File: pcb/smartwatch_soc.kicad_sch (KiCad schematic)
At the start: 37 parts, among them J1 Battery Socket, J2 USB_A, Q1 PN2222A, Q2 PN2222A, Q3 PN2222A, SW1 EN_Switch, SW2 Button, SW3 Button, SW4 Button, SW5 Button, U1 ESP32-S3-MINI-1U, U2 LSM6DS3, U3 OLED_Display, U5 CP2102N-Axx-xQFN20

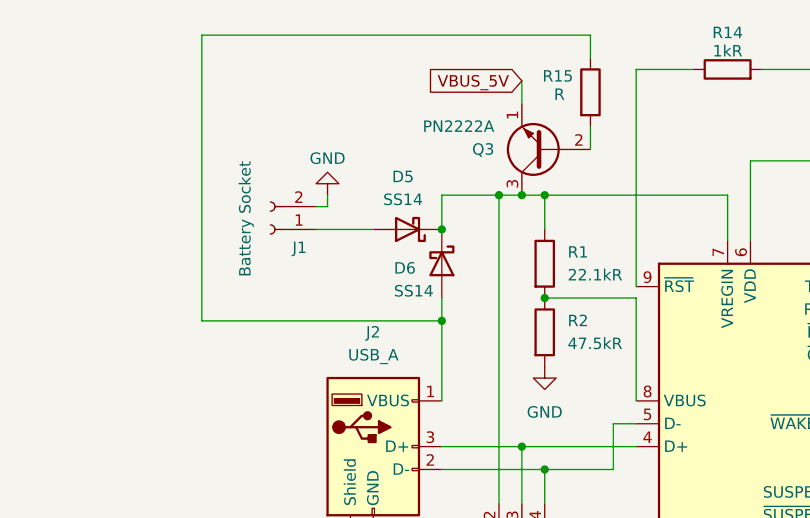
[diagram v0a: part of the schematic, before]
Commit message: use tht instead of smd for resistors, capacitors
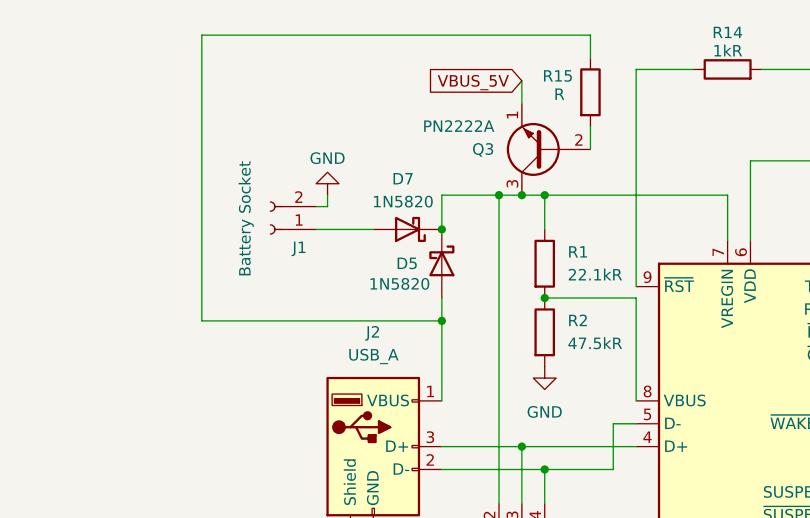
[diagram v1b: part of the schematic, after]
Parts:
- removed D5, D6: SS14, Diode_SMD:D_SMA, symbol Diode:SS14
- added D5, D7: 1N5820, Diode_THT:D_DO-201AD_P15.24mm_Horizontal, symbol Diode:1N5820
- D2, D3, D4: footprint LED_SMD:LED_0201_0603Metric -> LED_THT:LED_D2.0mm_W4.0mm_H2.8mm_FlatTop
- R1, R10, R11, R12, R13, R14, R15, R2, R3, R4, R5, R6, R7, R8, R9: footprint Resistor_SMD:R_0201_0603Metric -> Resistor_THT:R_Axial_DIN0204_L3.6mm_D1.6mm_P2.54mm_Vertical
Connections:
- net at D1.2 (K), Q3.3 (C), R1.1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: now also D5.1 (K), D7.1 (K)
- net at J1.1 (Pin_1): now also D7.2 (A)
- net at J2.1 (VBUS), R15.1: now also D5.2 (A)
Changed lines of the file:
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@@
 	)
 	(junction
+		(at 161.29 35.56)
+		(diameter 0)
+		(color 0 0 0 0)
+	)
+	(junction
 		(at 238.76 144.78)
 		(diameter 0)
@@
 	)
 	(junction
-		(at 161.29 35.56)
-		(diameter 0)
-		(color 0 0 0 0)
-	)
-	(junction
 		(at 73.66 167.64)
 		(diameter 0)
@@
 			)
 		)
-		(property "Footprint" "LED_SMD:LED_0201_0603Metric"
+		(property "Footprint" "LED_THT:LED_D2.0mm_W4.0mm_H2.8mm_FlatTop"
 			(at 256.54 144.78 0)
 			(effects
@@
 			)
 		)
-		(property "Footprint" "Resistor_SMD:R_0201_0603Metric"
+		(property "Footprint" "Resistor_THT:R_Axial_DIN0204_L3.6mm_D1.6mm_P2.54mm_Vertical"
 			(at 71.882 173.99 90)
 			(effects
@@
 	)
 	(symbol
-		(lib_id "Diode:SS14")
-		(at 157.48 35.56 180)
-		(unit 1)
-		(exclude_from_sim no)
-		(in_bom yes)
-		(on_board yes)
-		(dnp no)
-		(property "Reference" "D5"
-			(at 156.972 29.718 0)
-			(effects
-				(font
-					(size 1.27 1.27)
-				)
-			)
-		)
-		(property "Value" "SS14"
-			(at 156.972 32.258 0)
-			(effects
-				(font
-					(size 1.27 1.27)
-				)
-			)
-		)
-		(property "Footprint" "Diode_SMD:D_SMA"
-			(at 157.48 31.115 0)
-			(effects
-				(font
-					(size 1.27 1.27)
-				)
-				(hide yes)
-			)
-		)
-		(property "Datasheet" "https://www.vishay.com/docs/88746/ss12.pdf"
-			(at 157.48 35.56 0)
-			(effects
-				(font
-					(size 1.27 1.27)
-				)
-				(hide yes)
-			)
-		)
-		(property "Description" "40V 1A Schottky Diode, SMA"
-			(at 157.48 35.56 0)
-			(effects
-				(font
-					(size 1.27 1.27)
-				)
-				(hide yes)
-			)
-		)
-		(pin "2"
-		)
-		(pin "1"
-		)
-		(instances
-			(project ""
-				(path "/35fbcf8c-23e2-4364-8111-b69121d03e91"
-					(reference "D5")
-					(unit 1)
-				)
-			)
-		)
-	)
-	(symbol
 		(lib_id "Connector:USB_A")
 		(at 153.67 59.69 0)
@@
 			)
 		)
-		(property "Footprint" "Resistor_SMD:R_0201_0603Metric"
+		(property "Footprint" "Resistor_THT:R_Axial_DIN0204_L3.6mm_D1.6mm_P2.54mm_Vertical"
 			(at 170.942 46.99 90)
 			(effects
@@
 			)
 		)
-		(property "Footprint" "Resistor_SMD:R_0201_0603Metric"
+		(property "Footprint" "Resistor_THT:R_Axial_DIN0204_L3.6mm_D1.6mm_P2.54mm_Vertical"
 			(at 50.292 173.99 90)
 			(effects
@@
 			)
 		)
-		(property "Footprint" "Resistor_SMD:R_0201_0603Metric"
+		(property "Footprint" "Resistor_THT:R_Axial_DIN0204_L3.6mm_D1.6mm_P2.54mm_Vertical"
 			(at 214.63 66.548 90)
 			(effects
@@
 			)
 		)
-		(property "Footprint" "Resistor_SMD:R_0201_0603Metric"
+		(property "Footprint" "Resistor_THT:R_Axial_DIN0204_L3.6mm_D1.6mm_P2.54mm_Vertical"
 			(at 227.33 113.538 90)
 			(effects
@@
 			)
 		)
-		(property "Footprint" "Resistor_SMD:R_0201_0603Metric"
+		(property "Footprint" "Resistor_THT:R_Axial_DIN0204_L3.6mm_D1.6mm_P2.54mm_Vertical"
 			(at 29.972 173.99 90)
 			(effects
@@
 			)
 		)
-		(property "Footprint" "Resistor_SMD:R_0201_0603Metric"
+		(property "Footprint" "Resistor_THT:R_Axial_DIN0204_L3.6mm_D1.6mm_P2.54mm_Vertical"
 			(at 176.022 20.32 90)
 			(effects
@@
 			)
 		)
-		(property "Footprint" "Resistor_SMD:R_0201_0603Metric"
+		(property "Footprint" "Resistor_THT:R_Axial_DIN0204_L3.6mm_D1.6mm_P2.54mm_Vertical"
 			(at 248.92 107.188 90)
 			(effects
@@
 			)
 		)
-		(property "Footprint" "Resistor_SMD:R_0201_0603Metric"
+		(property "Footprint" "Resistor_THT:R_Axial_DIN0204_L3.6mm_D1.6mm_P2.54mm_Vertical"
 			(at 236.982 139.7 90)
 			(effects
@@
 			)
 		)
-		(property "Footprint" "Resistor_SMD:R_0201_0603Metric"
+		(property "Footprint" "Resistor_THT:R_Axial_DIN0204_L3.6mm_D1.6mm_P2.54mm_Vertical"
 			(at 170.942 39.37 90)
 			(effects
@@
 	)
 	(symbol
+		(lib_id "Diode:1N5820")
+		(at 161.29 39.37 270)
+		(unit 1)
+		(exclude_from_sim no)
+		(in_bom yes)
+		(on_board yes)
+		(dnp no)
+		(property "Reference" "D5"
+			(at 156.21 39.37 90)
+			(effects
+				(font
+					(size 1.27 1.27)
+				)
+				(justify left)
+			)
+		)
+		(property "Value" "1N5820"
+			(at 153.162 41.656 90)
+			(effects
+				(font
+					(size 1.27 1.27)
+				)
+				(justify left)
+			)
+		)
+		(property "Footprint" "Diode_THT:D_DO-201AD_P15.24mm_Horizontal"
+			(at 156.845 39.37 0)
+			(effects
+				(font
+					(size 1.27 1.27)
+				)
+				(hide yes)
+			)
+		)
+		(property "Datasheet" "http://www.vishay.com/docs/88526/1n5820.pdf"
+			(at 161.29 39.37 0)
+			(effects
+				(font
+					(size 1.27 1.27)
+				)
+				(hide yes)
+			)
+		)
+		(property "Description" "20V 3A Schottky Barrier Rectifier Diode, DO-201AD"
+			(at 161.29 39.37 0)
+			(effects
+				(font
+					(size 1.27 1.27)
+				)
+				(hide yes)
+			)
+		)
+		(pin "2"
+		)
+		(pin "1"
+		)
+		(instances
+			(project "smartwatch_soc"
+				(path "/35fbcf8c-23e2-4364-8111-b69121d03e91"
+					(reference "D5")
+					(unit 1)
+				)
+			)
+		)
+	)
+	(symbol
 		(lib_id "Connector:Conn_01x02_Socket")
 		(at 142.24 35.56 180)
@@
 			)
 		)
-		(property "Footprint" "Resistor_SMD:R_0201_0603Metric"
+		(property "Footprint" "Resistor_THT:R_Axial_DIN0204_L3.6mm_D1.6mm_P2.54mm_Vertical"
 			(at 248.92 146.558 90)
 			(effects
@@
 			)
 		)
-		(property "Footprint" "Resistor_SMD:R_0201_0603Metric"
+		(property "Footprint" "Resistor_THT:R_Axial_DIN0204_L3.6mm_D1.6mm_P2.54mm_Vertical"
 			(at 227.33 152.908 90)
 			(effects
@@
 			)
 		)
-		(property "Footprint" "Resistor_SMD:R_0201_0603Metric"
+		(property "Footprint" "Resistor_THT:R_Axial_DIN0204_L3.6mm_D1.6mm_P2.54mm_Vertical"
 			(at 92.202 173.99 90)
 			(effects
@@
 			)
 		)
-		(property "Footprint" "LED_SMD:LED_0201_0603Metric"
+		(property "Footprint" "LED_THT:LED_D2.0mm_W4.0mm_H2.8mm_FlatTop"
 			(at 256.54 105.41 0)
 			(effects
@@
 	)
 	(symbol
-		(lib_id "Diode:SS14")
-		(at 161.29 39.37 270)
-		(unit 1)
-		(exclude_from_sim no)
-		(in_bom yes)
-		(on_board yes)
-		(dnp no)
-		(property "Reference" "D6"
-			(at 155.956 39.878 90)
-			(effects
-				(font
-					(size 1.27 1.27)
-				)
-				(justify left)
-			)
-		)
-		(property "Value" "SS14"
-			(at 155.956 42.418 90)
-			(effects
-				(font
-					(size 1.27 1.27)
-				)
-				(justify left)
-			)
-		)
-		(property "Footprint" "Diode_SMD:D_SMA"
-			(at 156.845 39.37 0)
-			(effects
-				(font
-					(size 1.27 1.27)
-				)
-				(hide yes)
-			)
-		)
-		(property "Datasheet" "https://www.vishay.com/docs/88746/ss12.pdf"
-			(at 161.29 39.37 0)
-			(effects
-				(font
-					(size 1.27 1.27)
-				)
-				(hide yes)
-			)
-		)
-		(property "Description" "40V 1A Schottky Diode, SMA"
-			(at 161.29 39.37 0)
-			(effects
-				(font
-					(size 1.27 1.27)
-				)
-				(hide yes)
-			)
-		)
-		(pin "2"
-		)
-		(pin "1"
-		)
-		(instances
-			(project "smartwatch_soc"
-				(path "/35fbcf8c-23e2-4364-8111-b69121d03e91"
-					(reference "D6")
-					(unit 1)
-				)
-			)
-		)
-	)
-	(symbol
 		(lib_id "Switch:CK_KMS2xxG")
 		(at 73.66 160.02 90)
@@
 			)
 		)
-		(property "Footprint" "Resistor_SMD:R_0201_0603Metric"
+		(property "Footprint" "Resistor_THT:R_Axial_DIN0204_L3.6mm_D1.6mm_P2.54mm_Vertical"
 			(at 193.04 19.558 90)
 			(effects
@@
 			)
 		)
-		(property "Footprint" "LED_SMD:LED_0201_0603Metric"
+		(property "Footprint" "LED_THT:LED_D2.0mm_W4.0mm_H2.8mm_FlatTop"
 			(at 222.25 64.77 0)
 			(effects
@@
 			)
 		)
-		(property "Footprint" "Resistor_SMD:R_0201_0603Metric"
+		(property "Footprint" "Resistor_THT:R_Axial_DIN0204_L3.6mm_D1.6mm_P2.54mm_Vertical"
 			(at 236.982 100.33 90)
 			(effects
@@
 					(unit 1)
 				)
+			)
+		)
+	)
+	(symbol
+		(lib_id "Diode:1N5820")
+		(at 157.48 35.56 180)
+		(unit 1)
+		(exclude_from_sim no)
+		(in_bom yes)
+		(on_board yes)
+		(dnp no)
+		(property "Reference" "D7"
+			(at 156.972 29.972 0)
+			(effects
+				(font
+					(size 1.27 1.27)
+				)
+			)
+		)
+		(property "Value" "1N5820"
+			(at 156.972 32.512 0)
+			(effects
+				(font
+					(size 1.27 1.27)
+				)
+			)
+		)
+		(property "Footprint" "Diode_THT:D_DO-201AD_P15.24mm_Horizontal"
+			(at 157.48 31.115 0)
+			(effects
+				(font
+					(size 1.27 1.27)
+				)
+				(hide yes)
+			)
+		)
+		(property "Datasheet" "http://www.vishay.com/docs/88526/1n5820.pdf"
+			(at 157.48 35.56 0)
+			(effects
+				(font
+					(size 1.27 1.27)
+				)
+				(hide yes)
+			)
+		)
+		(property "Description" "20V 3A Schottky Barrier Rectifier Diode, DO-201AD"
+			(at 157.48 35.56 0)
+			(effects
+				(font
+					(size 1.27 1.27)
+				)
+				(hide yes)
+			)
+		)
+		(pin "2"
+		)
+		(pin "1"
+		)
+		(instances
+			(project ""
+				(path "/35fbcf8c-23e2-4364-8111-b69121d03e91"
+					(reference "D7")
+					(unit 1)
+				)

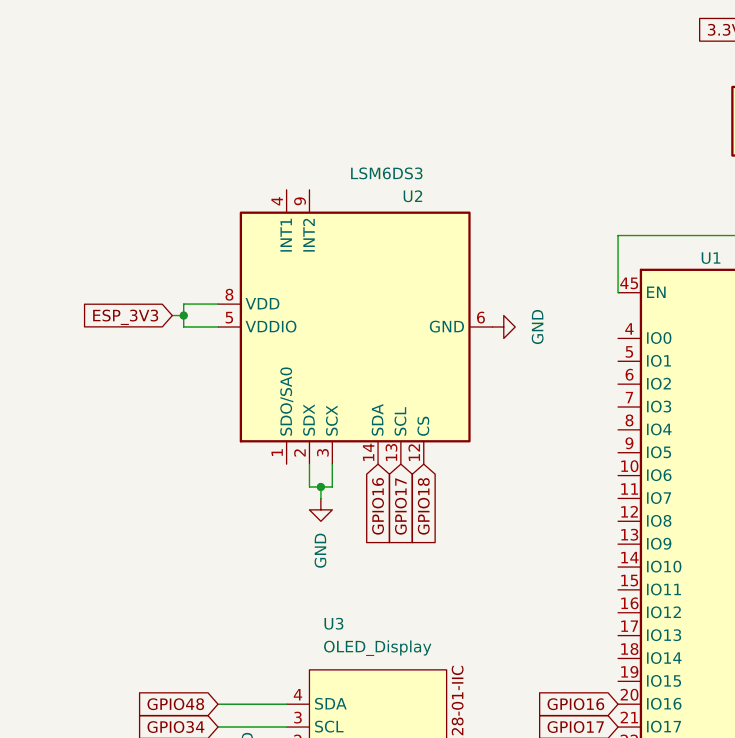
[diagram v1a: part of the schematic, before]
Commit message: added decoupling capacitors for accelerometer
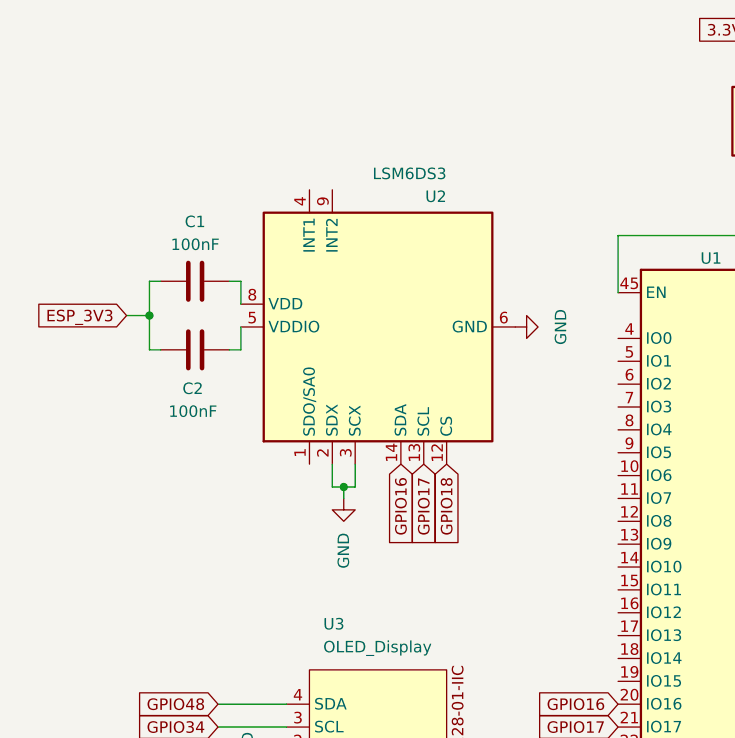
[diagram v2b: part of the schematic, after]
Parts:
- added C1, C2: 100nF, symbol Device:C
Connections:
- net ESP_3V3: now also C1.1, C2.1; no longer U2.5 (VDDIO), U2.8 (VDD)
- new net: C2.2, U2.5 (VDDIO)
- new net: C1.2, U2.8 (VDD)
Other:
- moved on the sheet: U2
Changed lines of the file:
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@@
 	)
 	(junction
-		(at 46.99 104.14)
+		(at 49.53 104.14)
 		(diameter 0)
 		(color 0 0 0 0)
 	)
 	(junction
-		(at 31.75 85.09)
+		(at 27.94 85.09)
 		(diameter 0)
 		(color 0 0 0 0)
@@
 	(wire
 		(pts
-			(xy 46.99 105.41) (xy 46.99 104.14)
+			(xy 49.53 105.41) (xy 49.53 104.14)
 		)
 		(stroke
@@
 	(wire
 		(pts
-			(xy 48.26 101.6) (xy 48.26 104.14)
+			(xy 50.8 101.6) (xy 50.8 104.14)
 		)
 		(stroke
@@
 	(wire
 		(pts
-			(xy 45.72 104.14) (xy 46.99 104.14)
+			(xy 48.26 104.14) (xy 49.53 104.14)
 		)
 		(stroke
@@
 	(wire
 		(pts
-			(xy 35.56 86.36) (xy 31.75 86.36)
+			(xy 38.1 88.9) (xy 36.83 88.9)
 		)
 		(stroke
@@
 	(wire
 		(pts
+			(xy 38.1 88.9) (xy 38.1 86.36)
+		)
+		(stroke
+			(width 0)
+			(type default)
+		)
+	)
+	(wire
+		(pts
 			(xy 116.84 86.36) (xy 118.11 86.36)
 		)
@@
 	(wire
 		(pts
-			(xy 31.75 85.09) (xy 31.75 86.36)
+			(xy 27.94 85.09) (xy 27.94 88.9)
 		)
 		(stroke
@@
 	(wire
 		(pts
-			(xy 31.75 83.82) (xy 35.56 83.82)
+			(xy 27.94 81.28) (xy 29.21 81.28)
 		)
 		(stroke
@@
 	(wire
 		(pts
-			(xy 31.75 83.82) (xy 31.75 85.09)
+			(xy 27.94 81.28) (xy 27.94 85.09)
+		)
+		(stroke
+			(width 0)
+			(type default)
+		)
+	)
+	(wire
+		(pts
+			(xy 36.83 81.28) (xy 38.1 81.28)
 		)
 		(stroke
@@
 	(wire
 		(pts
-			(xy 31.75 85.09) (xy 30.48 85.09)
+			(xy 27.94 85.09) (xy 25.4 85.09)
 		)
 		(stroke
@@
 	(wire
 		(pts
-			(xy 48.26 104.14) (xy 46.99 104.14)
+			(xy 50.8 104.14) (xy 49.53 104.14)
 		)
 		(stroke
@@
 	(wire
 		(pts
-			(xy 45.72 101.6) (xy 45.72 104.14)
+			(xy 48.26 101.6) (xy 48.26 104.14)
 		)
 		(stroke
@@
 	(wire
 		(pts
+			(xy 38.1 81.28) (xy 38.1 83.82)
+		)
+		(stroke
+			(width 0)
+			(type default)
+		)
+	)
+	(wire
+		(pts
 			(xy 153.67 69.85) (xy 153.67 76.2)
 		)
@@
 	(wire
 		(pts
+			(xy 29.21 88.9) (xy 27.94 88.9)
+		)
+		(stroke
+			(width 0)
+			(type default)
+		)
+	)
+	(wire
+		(pts
 			(xy 52.07 151.13) (xy 52.07 154.94)
 		)
@@
 	(global_label "GPIO18"
 		(shape input)
-		(at 58.42 101.6 270)
+		(at 60.96 101.6 270)
 		(fields_autoplaced yes)
 		(effects
@@
 		)
 		(property "Intersheetrefs" "${INTERSHEET_REFS}"
-			(at 58.42 111.4795 90)
+			(at 60.96 111.4795 90)
 			(effects
 				(font
@@
 	(global_label "GPIO17"
 		(shape input)
-		(at 55.88 101.6 270)
+		(at 58.42 101.6 270)
 		(fields_autoplaced yes)
 		(effects
@@
 		)
 		(property "Intersheetrefs" "${INTERSHEET_REFS}"
-			(at 55.88 111.4795 90)
+			(at 58.42 111.4795 90)
 			(effects
 				(font
@@
 	(global_label "GPIO16"
 		(shape input)
-		(at 53.34 101.6 270)
+		(at 55.88 101.6 270)
 		(fields_autoplaced yes)
 		(effects
@@
 		)
 		(property "Intersheetrefs" "${INTERSHEET_REFS}"
-			(at 53.34 111.4795 90)
+			(at 55.88 111.4795 90)
 			(effects
 				(font
@@
 	(global_label "ESP_3V3"
 		(shape input)
-		(at 30.48 85.09 180)
+		(at 25.4 85.09 180)
 		(fields_autoplaced yes)
 		(effects
@@
 		)
 		(property "Intersheetrefs" "${INTERSHEET_REFS}"
-			(at 19.3911 85.09 0)
+			(at 14.3111 85.09 0)
 			(effects
 				(font
@@
 	)
 	(symbol
+		(lib_id "Device:C")
+		(at 33.02 88.9 90)
+		(unit 1)
+		(exclude_from_sim no)
+		(in_bom yes)
+		(on_board yes)
+		(dnp no)
+		(property "Reference" "C2"
+			(at 32.766 93.218 90)
+			(effects
+				(font
+					(size 1.27 1.27)
+				)
+			)
+		)
+		(property "Value" "100nF"
+			(at 32.766 95.758 90)
+			(effects
+				(font
+					(size 1.27 1.27)
+				)
+			)
+		)
+		(property "Footprint" ""
+			(at 36.83 87.9348 0)
+			(effects
+				(font
+					(size 1.27 1.27)
+				)
+				(hide yes)
+			)
+		)
+		(property "Datasheet" "~"
+			(at 33.02 88.9 0)
+			(effects
+				(font
+					(size 1.27 1.27)
+				)
+				(hide yes)
+			)
+		)
+		(property "Description" "Unpolarized capacitor"
+			(at 33.02 88.9 0)
+			(effects
+				(font
+					(size 1.27 1.27)
+				)
+				(hide yes)
+			)
+		)
+		(pin "2"
+		)
+		(pin "1"
+		)
+		(instances
+			(project "smartwatch_soc"
+				(path "/35fbcf8c-23e2-4364-8111-b69121d03e91"
+					(reference "C2")
+					(unit 1)
+				)
+			)
+		)
+	)
+	(symbol
 		(lib_id "Device:R")
 		(at 227.33 111.76 90)
@@
 	(symbol
 		(lib_id "Sensor_Motion:LSM6DS3")
-		(at 50.8 86.36 90)
+		(at 53.34 86.36 90)
 		(unit 1)
 		(exclude_from_sim no)
@@
 		(dnp no)
 		(property "Reference" "U2"
-			(at 58.42 71.882 90)
+			(at 60.96 71.882 90)
 			(effects
 				(font
@@
 		)
 		(property "Value" "LSM6DS3"
-			(at 58.42 69.342 90)
+			(at 60.96 69.342 90)
 			(effects
 				(font
@@
 		)
 		(property "Footprint" "Package_LGA:LGA-14_3x2.5mm_P0.5mm_LayoutBorder3x4y"
-			(at 68.58 96.52 0)
+			(at 71.12 96.52 0)
 			(effects
 				(font
@@
 		)
 		(property "Datasheet" "https://www.st.com/resource/en/datasheet/lsm6ds3tr-c.pdf"
-			(at 67.31 83.82 0)
+			(at 69.85 83.82 0)
 			(effects
 				(font
@@
 		)
 		(property "Description" "I2C/SPI, iNEMO inertial module: always-on 3D accelerometer and 3D gyroscope"
-			(at 50.8 86.36 0)
+			(at 53.34 86.36 0)
 			(effects
 				(font
@@
 	(symbol
 		(lib_id "power:GND")
-		(at 46.99 105.41 0)
+		(at 49.53 105.41 0)
 		(unit 1)
 		(exclude_from_sim no)
@@
 		(fields_autoplaced yes)
 		(property "Reference" "#PWR011"
-			(at 46.99 111.76 0)
+			(at 49.53 111.76 0)
 			(effects
 				(font
@@
 		)
 		(property "Value" "GND"
-			(at 46.9899 109.22 90)
+			(at 49.5299 109.22 90)
 			(effects
 				(font
@@
 		)
 		(property "Footprint" ""
-			(at 46.99 105.41 0)
+			(at 49.53 105.41 0)
 			(effects
 				(font
@@
 		)
 		(property "Datasheet" ""
-			(at 46.99 105.41 0)
+			(at 49.53 105.41 0)
 			(effects
 				(font
@@
 		)
 		(property "Description" "Power symbol creates a global label with name \"GND\" , ground"
-			(at 46.99 105.41 0)
+			(at 49.53 105.41 0)
 			(effects
 				(font
@@
 	)
 	(symbol
+		(lib_id "Device:C")
+		(at 33.02 81.28 90)
+		(unit 1)
+		(exclude_from_sim no)
+		(in_bom yes)
+		(on_board yes)
+		(dnp no)
+		(property "Reference" "C1"
+			(at 33.02 74.676 90)
+			(effects
+				(font
+					(size 1.27 1.27)
+				)
+			)
+		)
+		(property "Value" "100nF"
+			(at 33.02 77.216 90)
+			(effects
+				(font
+					(size 1.27 1.27)
+				)
+			)
+		)
+		(property "Footprint" ""
+			(at 36.83 80.3148 0)
+			(effects
+				(font
+					(size 1.27 1.27)
+				)
+				(hide yes)
+			)
+		)
+		(property "Datasheet" "~"
+			(at 33.02 81.28 0)
+			(effects
+				(font
+					(size 1.27 1.27)
+				)
+				(hide yes)
+			)
+		)
+		(property "Description" "Unpolarized capacitor"
+			(at 33.02 81.28 0)
+			(effects
+				(font
+					(size 1.27 1.27)
+				)
+				(hide yes)
+			)
+		)
+		(pin "2"
+		)
+		(pin "1"
+		)
+		(instances
+			(project ""
+				(path "/35fbcf8c-23e2-4364-8111-b69121d03e91"
+					(reference "C1")
+					(unit 1)
+				)
+			)
+		)
+	)
+	(symbol
 		(lib_id "Switch:CK_KMS2xxG")
 		(at 73.66 160.02 90)
@@
 	(symbol
 		(lib_id "power:GND")
-		(at 66.04 86.36 90)
+		(at 68.58 86.36 90)
 		(unit 1)
 		(exclude_from_sim no)
@@
 		(dnp no)
 		(property "Reference" "#PWR03"
-			(at 72.39 86.36 0)
+			(at 74.93 86.36 0)
 			(effects
 				(font
@@
 		)
 		(property "Value" "GND"
-			(at 71.12 86.36 0)
+			(at 73.66 86.36 0)
 			(effects
 				(font
@@
 		)
 		(property "Footprint" ""
-			(at 66.04 86.36 0)
+			(at 68.58 86.36 0)
 			(effects
 				(font
@@
 		)
 		(property "Datasheet" ""
-			(at 66.04 86.36 0)
+			(at 68.58 86.36 0)
 			(effects
 				(font
@@
 		)
 		(property "Description" "Power symbol creates a global label with name \"GND\" , ground"
-			(at 66.04 86.36 0)
+			(at 68.58 86.36 0)
 			(effects
 				(font
